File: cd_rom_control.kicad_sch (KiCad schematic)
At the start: 113 parts, among them IC103 CXD1167Q, IC104 D78C14GF, IC105 D6378GF, IC106 D4364G, P7 Conn_01x07, Q102 24 30, Q105 Q_NPN_CBE, Q203 15 29, Q204 15 29, SW401 CD LID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

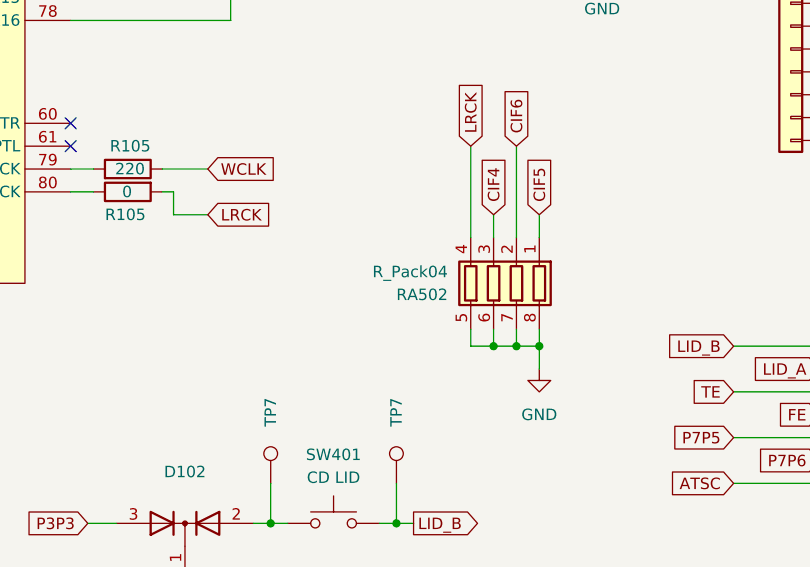
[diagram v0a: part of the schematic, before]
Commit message: Add more capacitor values, rearrange some schematics.
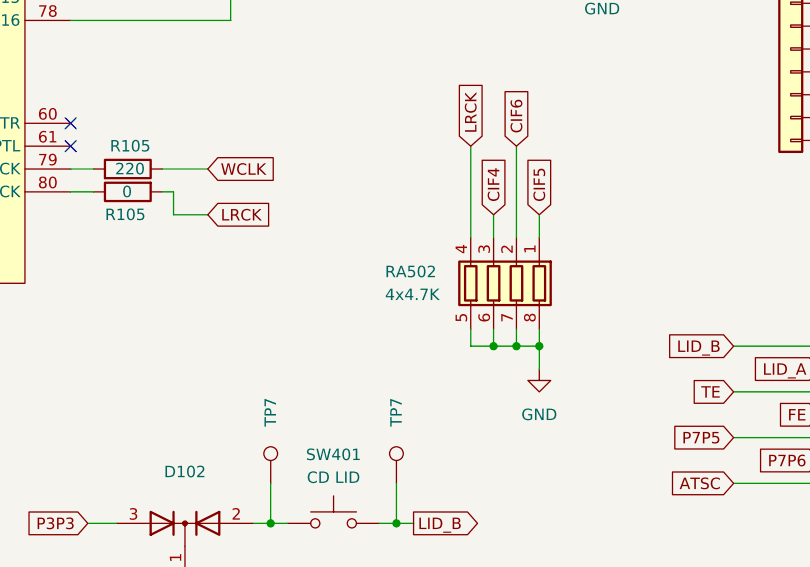
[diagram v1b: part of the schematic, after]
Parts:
- RA502: value R_Pack04 -> 4x4.7K
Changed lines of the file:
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@@
   )
   (symbol (lib_id "Device:R_Pack04") (at 224.155 240.665 180) (unit 1)
-    (in_bom yes) (on_board yes) (dnp no) (fields_autoplaced)
-    (property "Reference" "RA502" (at 219.075 241.935 0)
-      (effects (font (size 1.27 1.27)) (justify left))
+    (in_bom yes) (on_board yes) (dnp no)
+    (property "Reference" "RA502" (at 212.09 239.395 0)
+      (effects (font (size 1.27 1.27)) (justify right))
     )
-    (property "Value" "R_Pack04" (at 219.075 239.395 0)
-      (effects (font (size 1.27 1.27)) (justify left))
+    (property "Value" "4x4.7K" (at 212.09 241.935 0)
+      (effects (font (size 1.27 1.27)) (justify right))
     )
     (property "Footprint" "A-PCENGINE:R_Array_4x0603" (at 217.17 240.665 90)

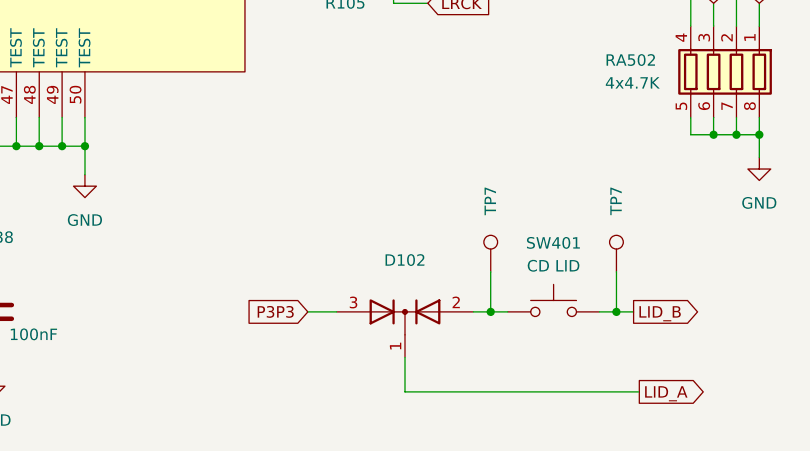
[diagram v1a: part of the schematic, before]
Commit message: Add markings for SMD Ds and Qs.
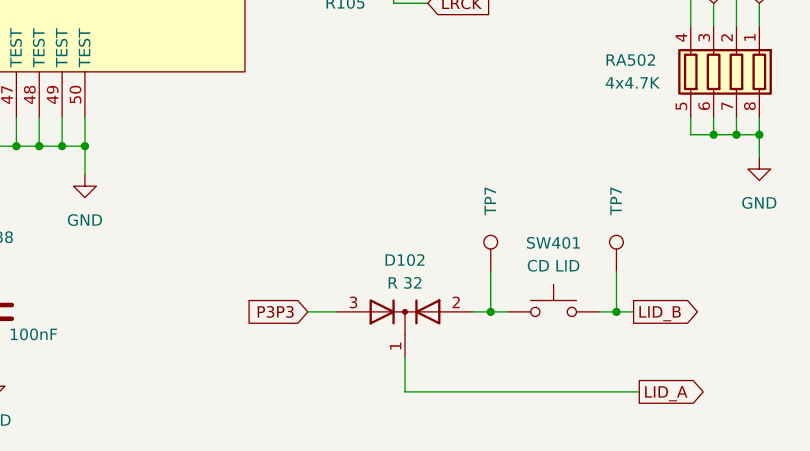
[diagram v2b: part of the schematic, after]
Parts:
- D102: value ~ -> R 32
- Q105: value Q_NPN_CBE -> 24 30
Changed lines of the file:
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@@
       (effects (font (size 1.27 1.27)))
     )
-    (property "Value" "~" (at 189.865 264.16 0)
+    (property "Value" "R 32" (at 189.865 264.16 0)
       (effects (font (size 1.27 1.27)))
     )
@@
       (effects (font (size 1.27 1.27)) (justify left))
     )
-    (property "Value" "Q_NPN_CBE" (at 49.53 62.23 0)
+    (property "Value" "24 30" (at 49.53 62.23 0)
       (effects (font (size 1.27 1.27)) (justify left) hide)
     )

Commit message: More schematic clean-up/annotation.
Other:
- note added: "DSP"
- note added: "This is a general purpose 8-bit microcontroller. Actual part is NEC μPD78C14, for which a datasheet is available."
- note added: "This is an NEC μPD6378. The NEC catalog lists this as a "CD ROM decoder LSI" which "Conforms to CD-ROM XA format". No datasheet found. Pin names are mostly derived from other chips."
- company: (none) -> By Cosam
- title: (none) -> PC Engine Duo CD-ROM Control
- moved on the sheet: C138, C951, R105, TP1, X101

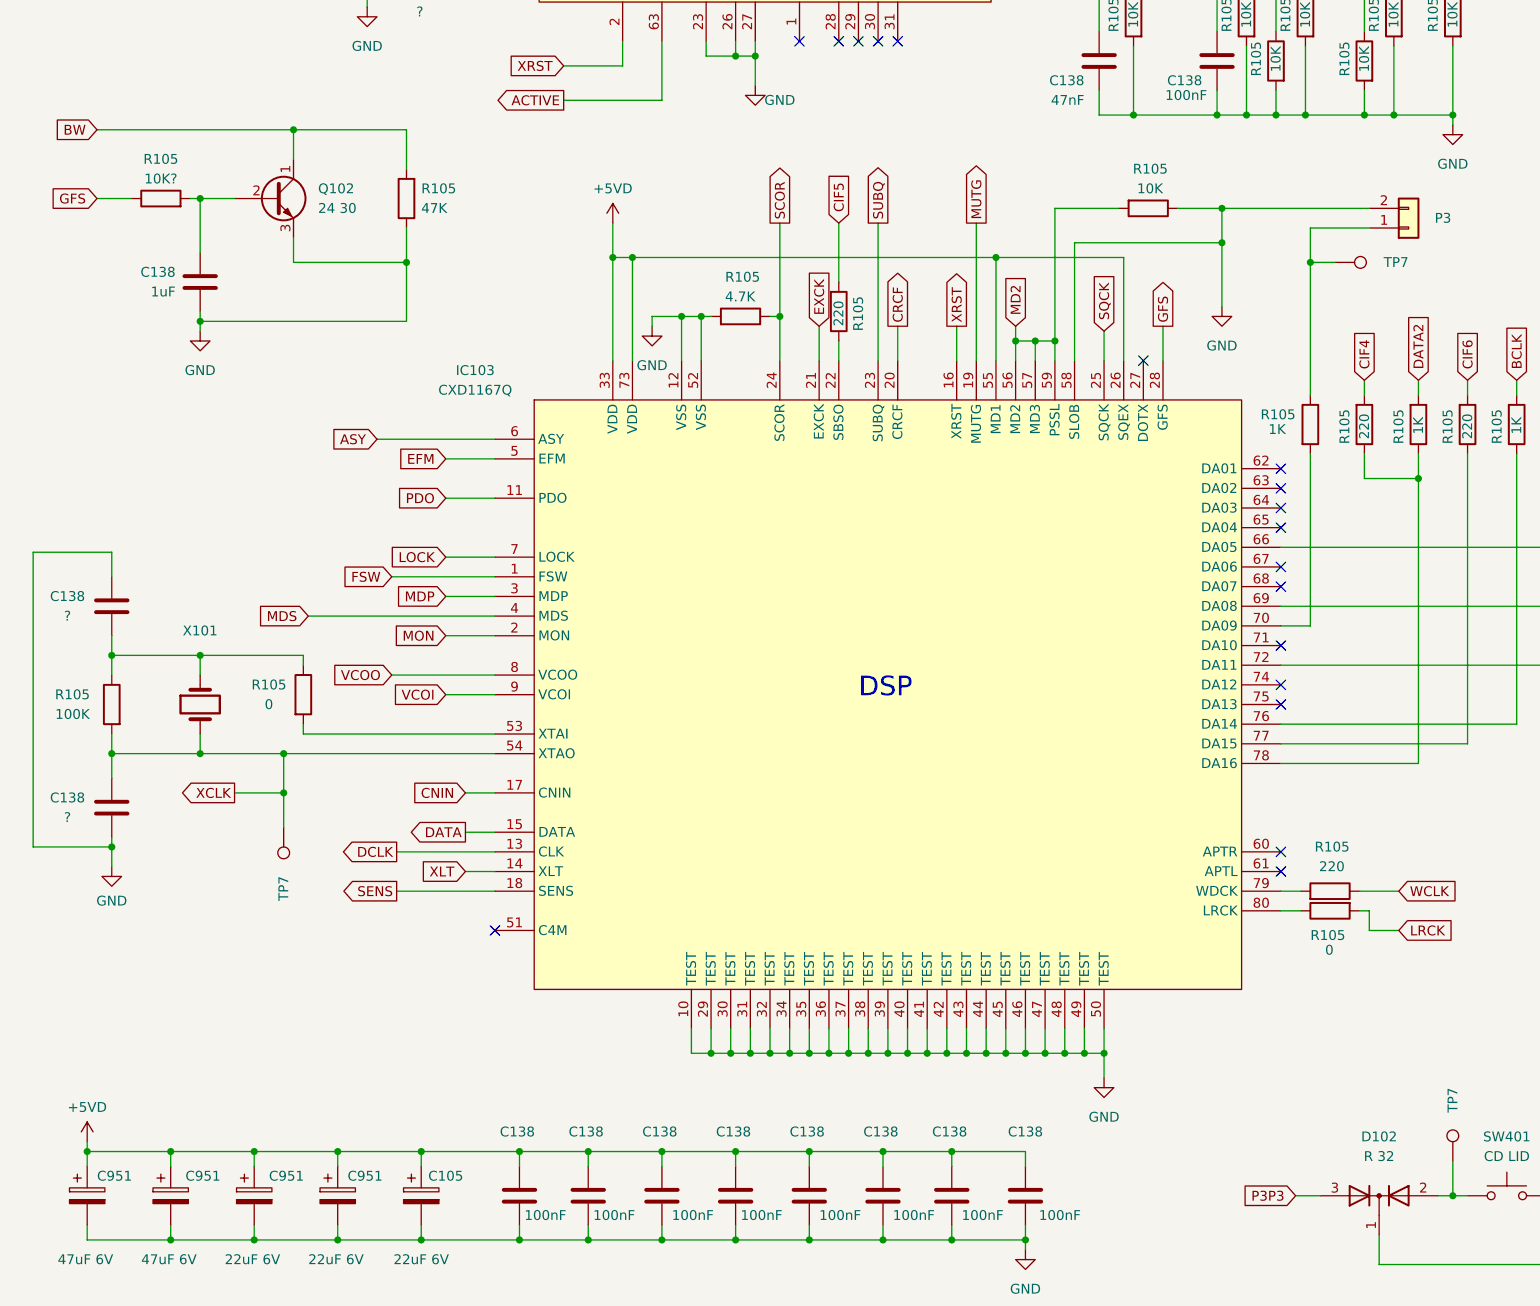
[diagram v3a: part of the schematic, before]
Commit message: Correct some values/references.
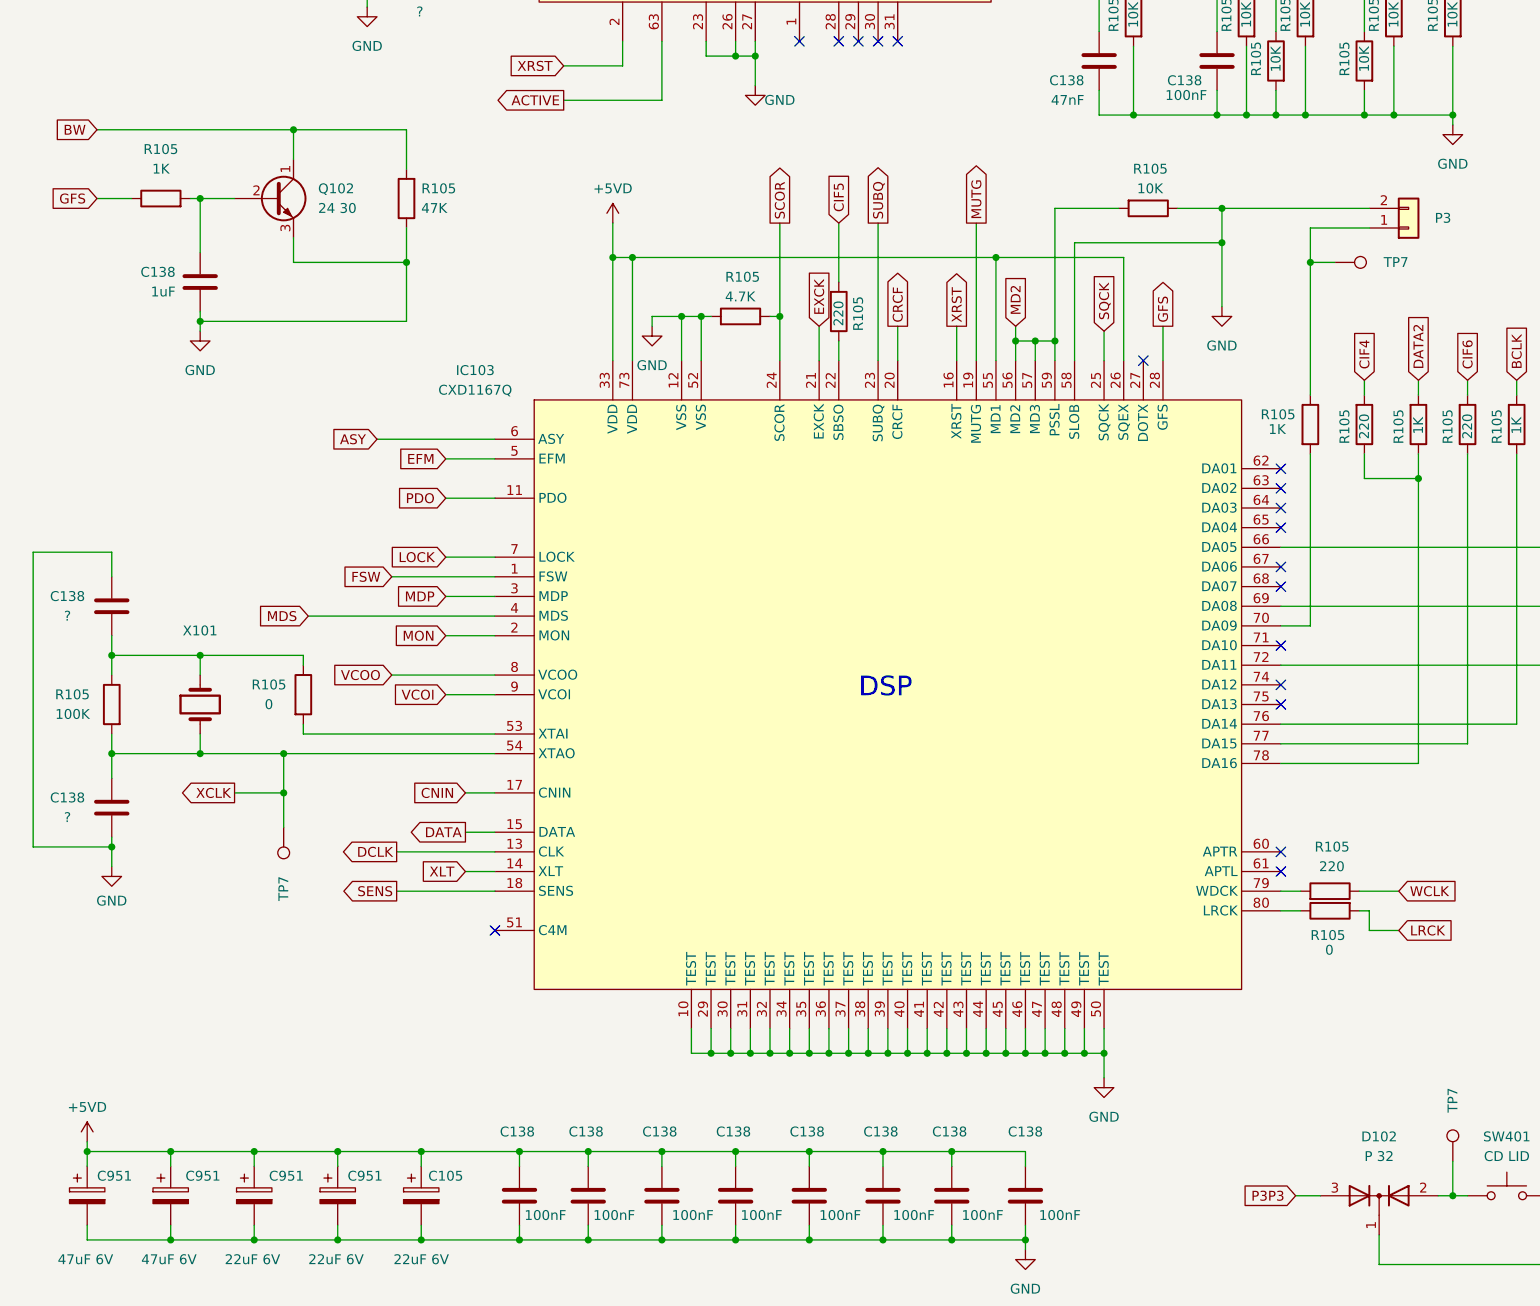
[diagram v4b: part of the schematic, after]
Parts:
- D102: value R 32 -> P 32
- R105: value 10K? -> 1K
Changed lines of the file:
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@@
   (symbol (lib_id "Device:R") (at 32.385 138.43 90) (unit 1)
     (in_bom yes) (on_board yes) (dnp no) (fields_autoplaced)
-    (property "Reference" "R105" (at 32.385 133.35 90)
-      (effects (font (size 1.27 1.27)))
-    )
-    (property "Value" "10K?" (at 32.385 135.89 90)
+    (property "Reference" "R105" (at 32.385 132.08 90)
+      (effects (font (size 1.27 1.27)))
+    )
+    (property "Value" "1K" (at 32.385 134.62 90)
       (effects (font (size 1.27 1.27)))
     )
@@
       (effects (font (size 1.27 1.27)))
     )
-    (property "Value" "R 32" (at 189.865 262.255 0)
-      (effects (font (size 1.27 1.27)))
-    )
+    (property "Value" "P 32" (at 189.865 262.255 0)
+      (effects (font (size 1.27 1.27)))
+    )

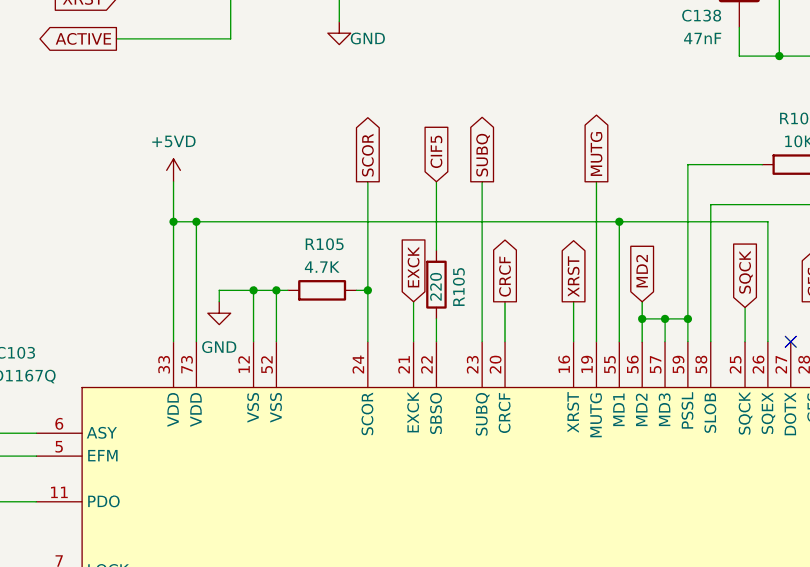
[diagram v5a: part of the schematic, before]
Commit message: Minor schematic/silkscreen changes.
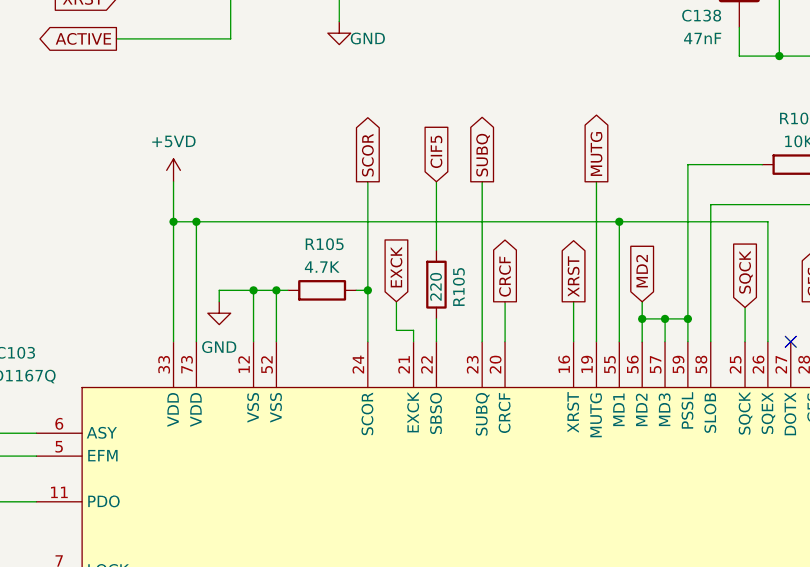
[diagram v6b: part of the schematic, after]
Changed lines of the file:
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@@
     (stroke (width 0) (type default))
   )
-  (wire (pts (xy 117.475 154.94) (xy 117.475 159.385))
+  (wire (pts (xy 115.57 154.94) (xy 115.57 158.115))
     (stroke (width 0) (type default))
   )
@@
     (stroke (width 0) (type default))
   )
+  (wire (pts (xy 115.57 158.115) (xy 117.475 158.115))
+    (stroke (width 0) (type default))
+  )
   (wire (pts (xy 387.985 208.915) (xy 387.35 208.915))
     (stroke (width 0) (type default))
@@
   )
   (wire (pts (xy 139.065 245.745) (xy 139.065 248.92))
+    (stroke (width 0) (type default))
+  )
+  (wire (pts (xy 117.475 158.115) (xy 117.475 159.385))
     (stroke (width 0) (type default))
   )
@@
     )
   )
-  (global_label "EXCK" (shape input) (at 117.475 154.94 90) (fields_autoplaced)
-    (effects (font (size 1.27 1.27)) (justify left))
-    (property "Intersheetrefs" "${INTERSHEET_REFS}" (at 117.475 147.0563 90)
-      (effects (font (size 1.27 1.27)) (justify left) hide)
-    )
+  (global_label "EXCK" (shape input) (at 115.57 154.94 90) (fields_autoplaced)
+    (effects (font (size 1.27 1.27)) (justify left))
+    (property "Intersheetrefs" "${INTERSHEET_REFS}" (at 115.57 147.0563 90)
+      (effects (font (size 1.27 1.27)) (justify left) hide)
+    )
